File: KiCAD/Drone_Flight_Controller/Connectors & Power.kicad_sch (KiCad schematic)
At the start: 35 parts, among them J301 Conn_01x03_Pin, J302 Conn_01x04, J303 Conn_01x03_Pin, J304 XT60, J305 Conn_01x03_Pin, J306 Conn_01x03_Pin, Q301 BC846C, Q302 BC846C, Q303 BC856C, Q304 BC846C, Q305 BC856C, Q306 BC856C, Q307 BC856C, Q309 BC846C, U202 AS358, U203 AS358, U301 AS358, U302 AS358, U305 AS358

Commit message: Export BOM
Export BOM
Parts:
- J301, J302, J303, J305, J306: now left out of the parts list
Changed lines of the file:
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@@
 		(unit 1)
 		(exclude_from_sim no)
-		(in_bom yes)
+		(in_bom no)
 		(on_board yes)
 		(dnp no)
@@
 		(unit 1)
 		(exclude_from_sim no)
-		(in_bom yes)
+		(in_bom no)
 		(on_board yes)
 		(dnp no)
@@
 		(unit 1)
 		(exclude_from_sim no)
-		(in_bom yes)
+		(in_bom no)
 		(on_board yes)
 		(dnp no)
@@
 		(unit 1)
 		(exclude_from_sim no)
-		(in_bom yes)
+		(in_bom no)
 		(on_board yes)
 		(dnp no)
@@
 		(unit 1)
 		(exclude_from_sim no)
-		(in_bom yes)
-		(on_board yes)
-		(dnp no)
+		(in_bom no)
+		(on_board yes)
+		(dnp no)

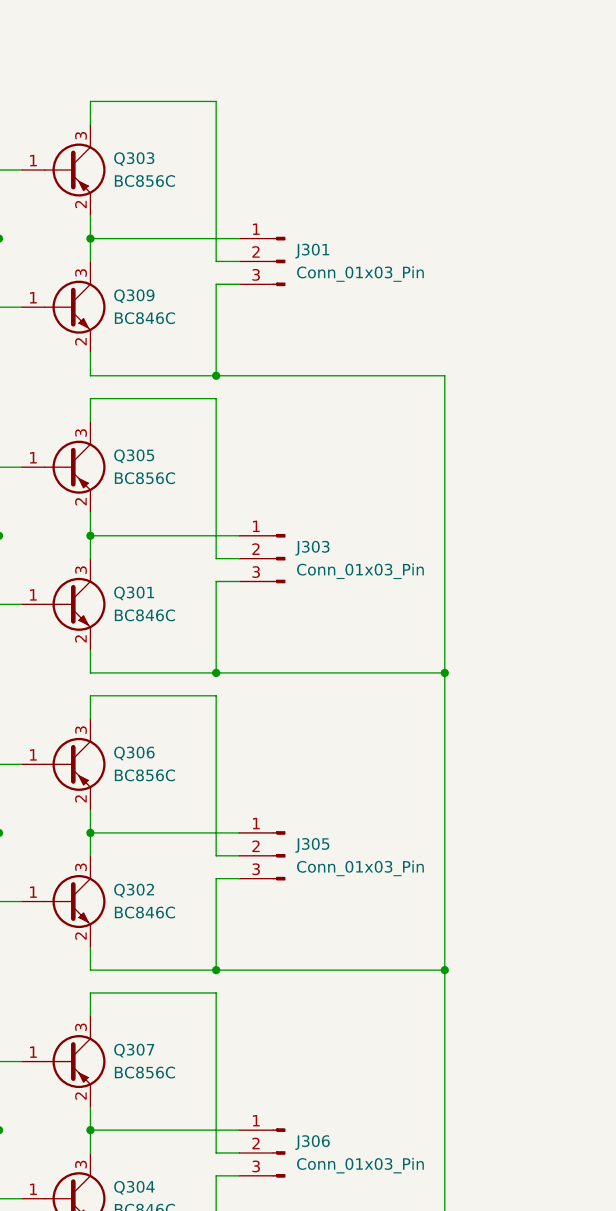
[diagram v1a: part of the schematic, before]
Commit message: Add +4V76 via BEC circuits and USB
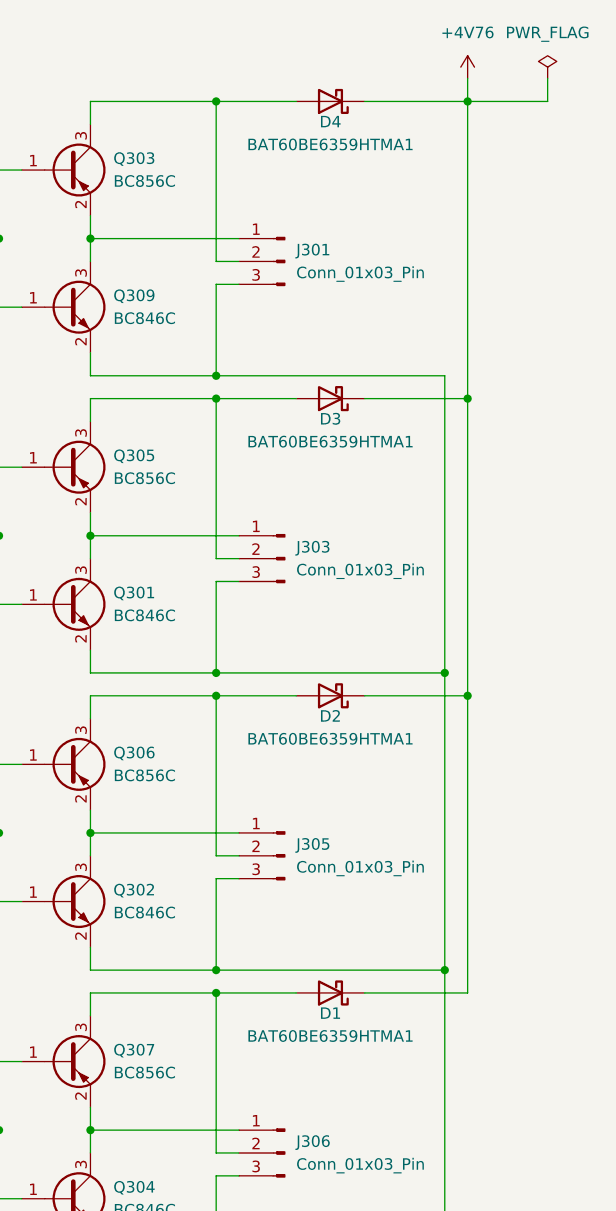
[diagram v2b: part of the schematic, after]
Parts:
- added D1, D2, D3, D4: BAT60BE6359HTMA1, Diode_SMD:D_SOD-323F, symbol Device:D_Schottky
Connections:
- net at J306.2 (Pin_2), Q307.3 (C): now also D1.2 (A)
- net at J303.2 (Pin_2), Q305.3 (C): now also D3.2 (A)
- net at J305.2 (Pin_2), Q306.3 (C): now also D2.2 (A)
- net at J301.2 (Pin_2), Q303.3 (C): now also D4.2 (A)
- new net +4V76: D1.1 (K), D2.1 (K), D3.1 (K), D4.1 (K)

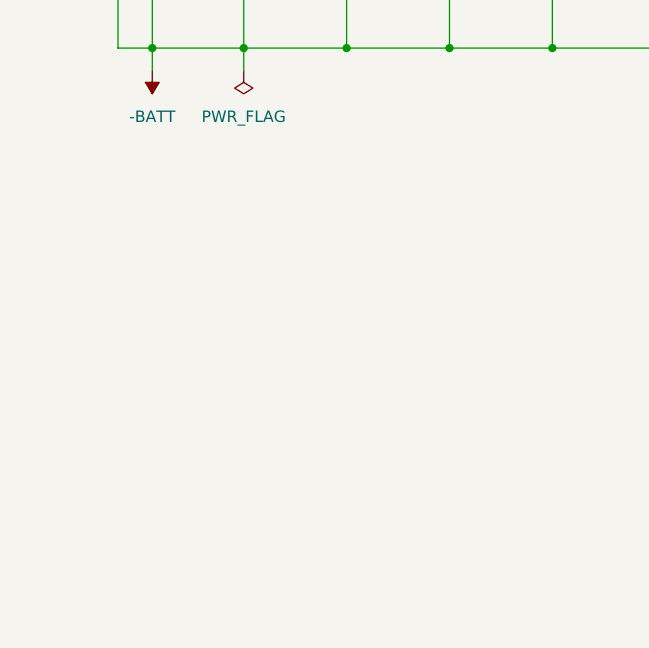
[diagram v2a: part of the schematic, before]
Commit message: Expose 3 GPIO Pins
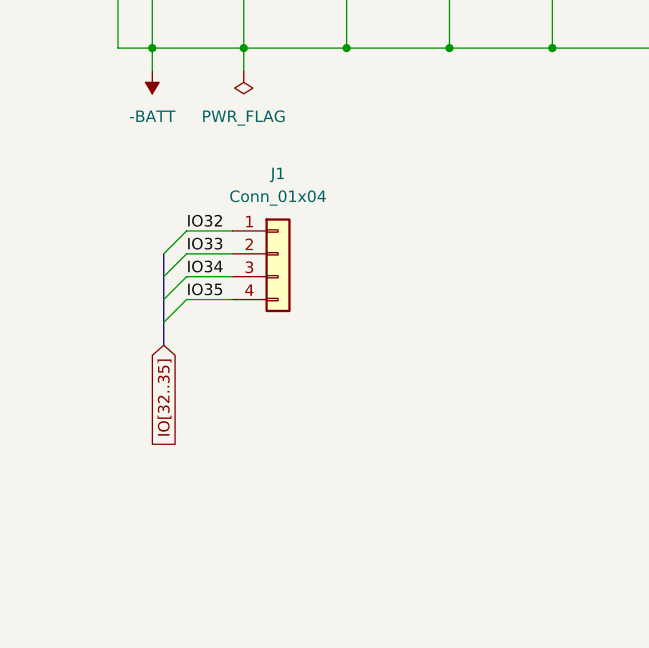
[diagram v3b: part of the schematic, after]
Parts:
- added J1: Conn_01x04, Connector_PinHeader_2.54mm:PinHeader_1x04_P2.54mm_Vertical, symbol Connector_Generic:Conn_01x04
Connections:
- new net IO32: J1.1 (Pin_1)
- new net IO33: J1.2 (Pin_2)
- new net IO34: J1.3 (Pin_3)
- new net IO35: J1.4 (Pin_4)
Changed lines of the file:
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@@
+	)
+	(bus_entry
+		(at 31.75 127)
+		(size 2.54 -2.54)
+		(stroke
+			(width 0)
+			(type default)
+		)
 	)
 	(bus_entry
@@
 	)
 	(bus_entry
+		(at 31.75 121.92)
+		(size 2.54 -2.54)
+		(stroke
+			(width 0)
+			(type default)
+		)
+	)
+	(bus_entry
 		(at 160.02 41.91)
 		(size -2.54 -2.54)
+		(stroke
+			(width 0)
+			(type default)
+		)
+	)
+	(bus_entry
+		(at 31.75 124.46)
+		(size 2.54 -2.54)
+		(stroke
+			(width 0)
+			(type default)
+		)
+	)
+	(bus_entry
+		(at 31.75 119.38)
+		(size 2.54 -2.54)
 		(stroke
 			(width 0)
@@
 	(wire
 		(pts
+			(xy 39.37 116.84) (xy 34.29 116.84)
+		)
+		(stroke
+			(width 0)
+			(type default)
+		)
+	)
+	(wire
+		(pts
 			(xy 30.48 31.75) (xy 41.91 31.75)
 		)
@@
 	(wire
 		(pts
+			(xy 39.37 124.46) (xy 34.29 124.46)
+		)
+		(stroke
+			(width 0)
+			(type default)
+		)
+	)
+	(wire
+		(pts
 			(xy 222.25 110.49) (xy 222.25 120.65)
 		)
@@
 		)
 	)
+	(bus
+		(pts
+			(xy 31.75 127) (xy 31.75 129.54)
+		)
+		(stroke
+			(width 0)
+			(type default)
+		)
+	)
 	(wire
 		(pts
@@
 		)
 	)
+	(bus
+		(pts
+			(xy 31.75 124.46) (xy 31.75 127)
+		)
+		(stroke
+			(width 0)
+			(type default)
+		)
+	)
 	(wire
 		(pts
@@
 		)
 	)
+	(bus
+		(pts
+			(xy 31.75 121.92) (xy 31.75 124.46)
+		)
+		(stroke
+			(width 0)
+			(type default)
+		)
+	)
+	(wire
+		(pts
+			(xy 39.37 121.92) (xy 34.29 121.92)
+		)
+		(stroke
+			(width 0)
+			(type default)
+		)
+	)
 	(wire
 		(pts
@@
 		)
 	)
+	(bus
+		(pts
+			(xy 31.75 119.38) (xy 31.75 121.92)
+		)
+		(stroke
+			(width 0)
+			(type default)
+		)
+	)
 	(wire
 		(pts
@@
 		(pts
 			(xy 157.48 36.83) (xy 157.48 39.37)
+		)
+		(stroke
+			(width 0)
+			(type default)
+		)
+	)
+	(wire
+		(pts
+			(xy 39.37 119.38) (xy 34.29 119.38)
 		)
 		(stroke
@@
 		)
 	)
+	(label "IO33"
+		(at 34.29 119.38 0)
+		(effects
+			(font
+				(size 1.27 1.27)
+			)
+			(justify left bottom)
+		)
+	)
 	(label "Motor3"
 		(at 161.29 41.91 0)
@@
 		)
 	)
+	(label "IO32"
+		(at 34.29 116.84 0)
+		(effects
+			(font
+				(size 1.27 1.27)
+			)
+			(justify left bottom)
+		)
+	)
+	(label "IO34"
+		(at 34.29 121.92 0)
+		(effects
+			(font
+				(size 1.27 1.27)
+			)
+			(justify left bottom)
+		)
+	)
 	(label "Motor1"
 		(at 161.29 36.83 0)
+		(effects
+			(font
+				(size 1.27 1.27)
+			)
+			(justify left bottom)
+		)
+	)
+	(label "IO35"
+		(at 34.29 124.46 0)
 		(effects
 			(font
@@
 				)
 				(justify left)
+				(hide yes)
+			)
+		)
+	)
+	(global_label "IO[32..35]"
+		(shape input)
+		(at 31.75 129.54 270)
+		(fields_autoplaced yes)
+		(effects
+			(font
+				(size 1.27 1.27)
+			)
+			(justify right)
+		)
+		(property "Intersheetrefs" "${INTERSHEET_REFS}"
+			(at 31.75 142.2015 90)
+			(effects
+				(font
+					(size 1.27 1.27)
+				)
+				(justify right)
 				(hide yes)
 			)
@@
 					(unit 1)
 				)
+			)
+		)
+	)
+	(symbol
+		(lib_id "Connector_Generic:Conn_01x04")
+		(at 44.45 119.38 0)
+		(unit 1)
+		(exclude_from_sim no)
+		(in_bom no)
+		(on_board yes)
+		(dnp no)
+		(property "Reference" "J1"
+			(at 44.45 110.49 0)
+			(effects
+				(font
+					(size 1.27 1.27)
+				)
+			)
+		)
+		(property "Value" "Conn_01x04"
+			(at 44.45 113.03 0)
+			(effects
+				(font
+					(size 1.27 1.27)
+				)
+			)
+		)
+		(property "Footprint" "Connector_PinHeader_2.54mm:PinHeader_1x04_P2.54mm_Vertical"
+			(at 44.45 119.38 0)
+			(effects
+				(font
+					(size 1.27 1.27)
+				)
+				(hide yes)
+			)
+		)
+		(property "Datasheet" "/"
+			(at 44.45 119.38 0)
+			(effects
+				(font
+					(size 1.27 1.27)
+				)
+				(hide yes)
+			)
+		)
+		(property "Description" "Generic connector, single row, 01x04, script generated (kicad-library-utils/schlib/autogen/connector/)"
+			(at 44.45 119.38 0)
+			(effects
+				(font
+					(size 1.27 1.27)
+				)
+				(hide yes)
+			)
+		)
+		(property "Link" "/"
+			(at 44.45 119.38 0)
+			(effects
+				(font
+					(size 1.27 1.27)
+				)
+				(hide yes)
+			)
+		)
+		(pin "3"
+		)
+		(pin "1"
+		)
+		(pin "2"
+		)
+		(pin "4"
+		)
+		(instances
+			(project "Drone_Flight_Controller"
+				(path "/05daaa24-e506-4b9a-9564-8bf799413ca8/260564b2-f35d-47a6-9418-8c7c5bce9239"
+					(reference "J1")
+					(unit 1)
+				)

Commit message: Remove unused connector
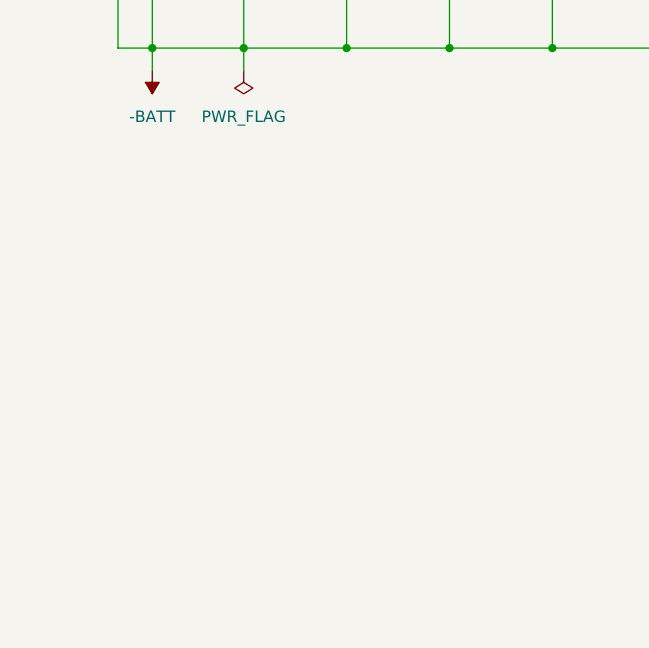
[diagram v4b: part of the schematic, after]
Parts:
- removed J1: Conn_01x04, Connector_PinHeader_2.54mm:PinHeader_1x04_P2.54mm_Vertical, symbol Connector_Generic:Conn_01x04

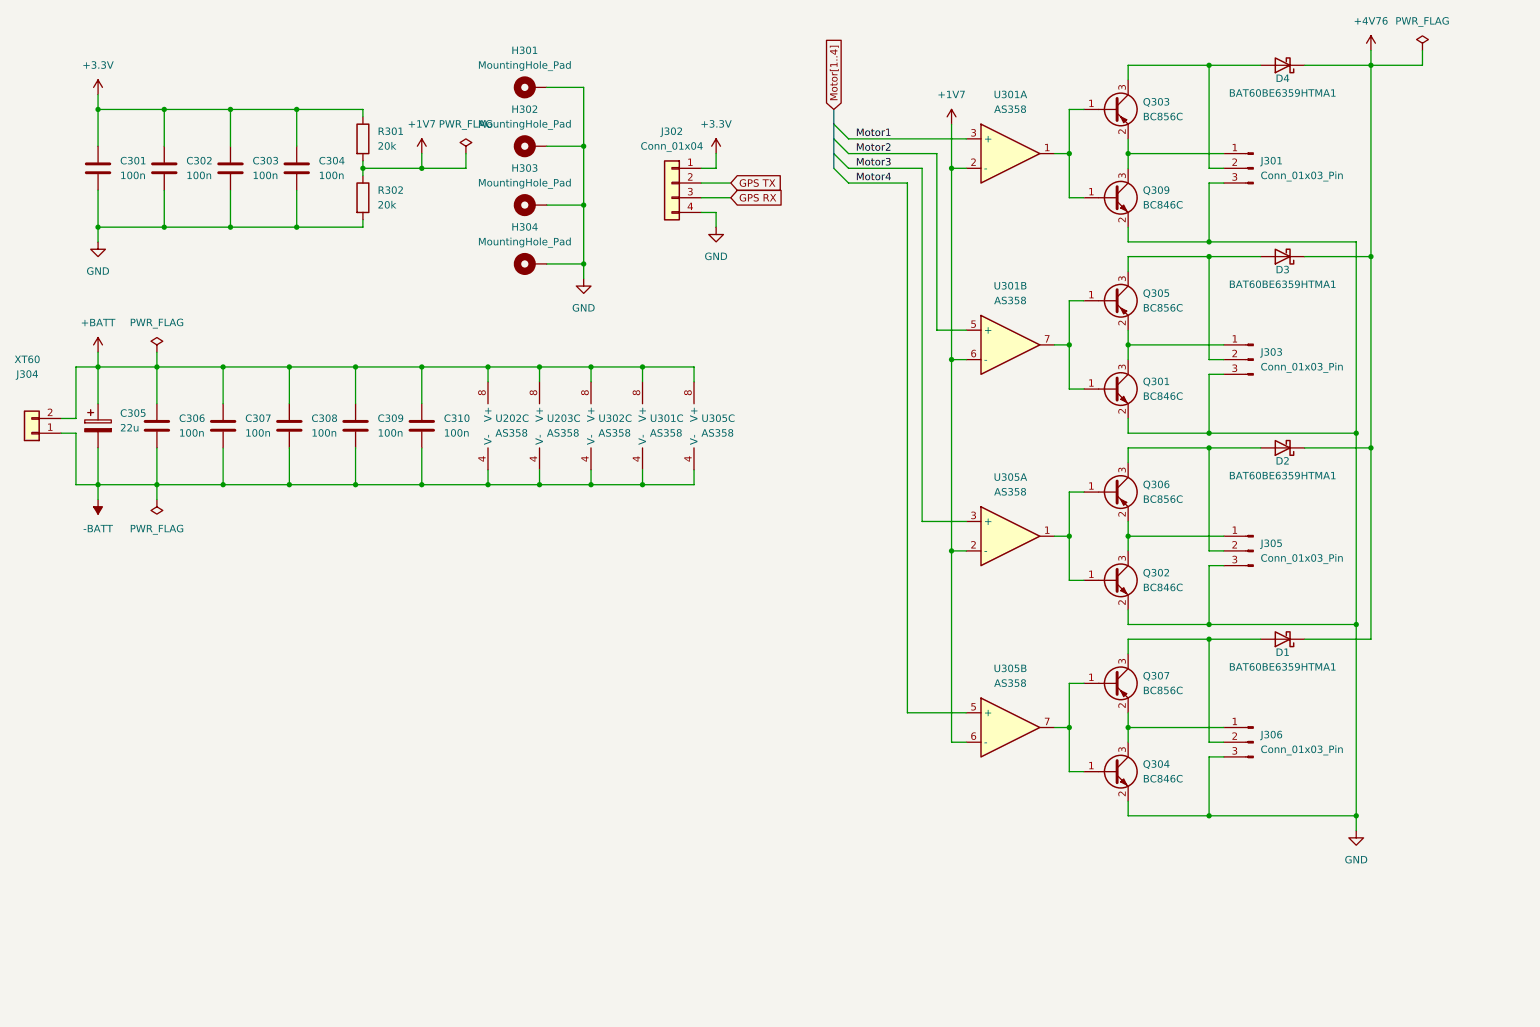
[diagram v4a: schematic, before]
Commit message: Fix ESC drivers
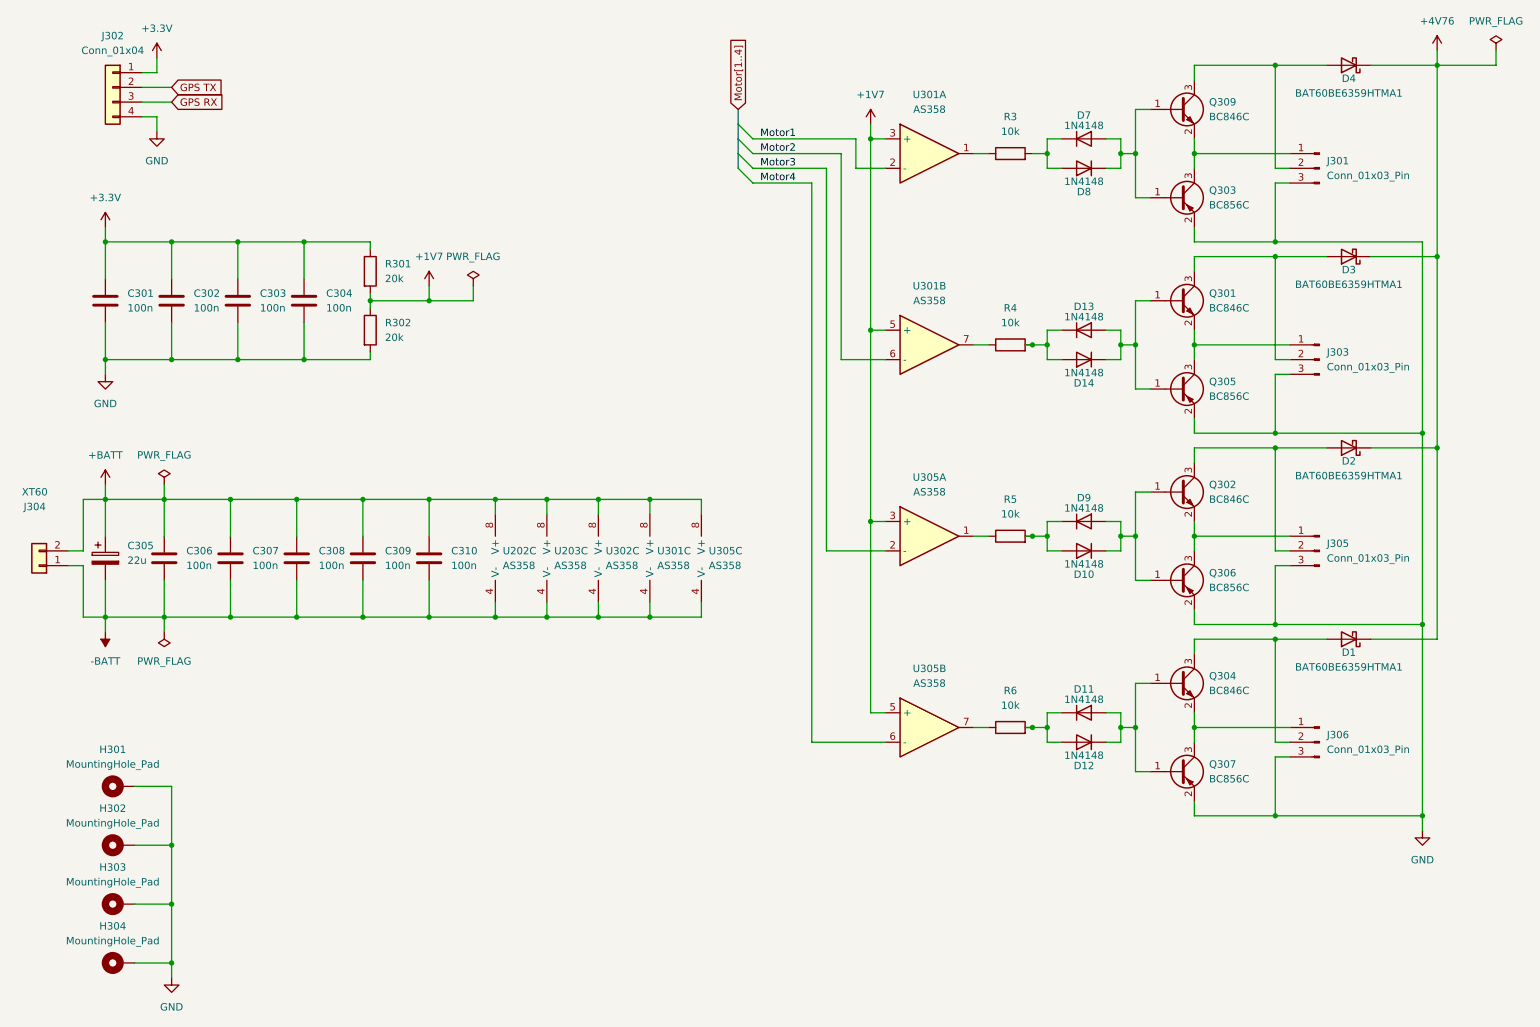
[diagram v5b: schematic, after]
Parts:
- added D10, D11, D12, D13, D14, D7, D8, D9: 1N4148, Diode_THT:D_DO-35_SOD27_P7.62mm_Horizontal, symbol Diode:1N4148
- added R3, R4, R5, R6: 10k, symbol Device:R
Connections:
- net +1V7: now also U301.3 (+), U301.5 (+), U305.3 (+), U305.5 (+); no longer U301.2 (-), U301.6 (-), U305.2 (-), U305.6 (-)
- net GND: now also Q303.2 (E), Q305.2 (E), Q306.2 (E), Q307.2 (E); no longer Q301.2 (E), Q302.2 (E), Q304.2 (E), Q309.2 (E)
- net Motor1: now also U301.2 (-); no longer U301.3 (+)
- net Motor2: now also U301.6 (-); no longer U301.5 (+)
- net Motor3: now also U305.2 (-); no longer U305.3 (+)
- net Motor4: now also U305.6 (-); no longer U305.5 (+)
- net at D1.2 (A), J306.2 (Pin_2): now also Q304.3 (C); no longer Q307.3 (C)
- net at Q303.1 (B), Q309.1 (B): now also D7.2 (A), D8.1 (K); no longer U301.1
- net at Q302.1 (B), Q306.1 (B): now also D10.1 (K), D9.2 (A); no longer U305.1
- net at Q304.1 (B), Q307.1 (B): now also D11.2 (A), D12.1 (K); no longer U305.7
- net at Q301.1 (B), Q305.1 (B): now also D13.2 (A), D14.1 (K); no longer U301.7
- net at D2.2 (A), J305.2 (Pin_2): now also Q302.3 (C); no longer Q306.3 (C)
- net at D4.2 (A), J301.2 (Pin_2): now also Q309.3 (C); no longer Q303.3 (C)
- net at D3.2 (A), J303.2 (Pin_2): now also Q301.3 (C); no longer Q305.3 (C)
- new net: R4.1, U301.7
- new net: D13.1 (K), D14.2 (A), R4.2
- new net: J301.1 (Pin_1), Q303.3 (C), Q309.2 (E)
- new net: D10.2 (A), D9.1 (K), R5.2
- new net: R5.1, U305.1
- new net: R6.1, U305.7
- new net: J306.1 (Pin_1), Q304.2 (E), Q307.3 (C)
- new net: J303.1 (Pin_1), Q301.2 (E), Q305.3 (C)
- new net: D11.1 (K), D12.2 (A), R6.2
- new net: J305.1 (Pin_1), Q302.2 (E), Q306.3 (C)
- new net: R3.1, U301.1
- new net: D7.1 (K), D8.2 (A), R3.2
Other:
- moved on the sheet: C301, C302, C303, C304, C305, C306, C307, C308, C309, C310, D1, D2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
